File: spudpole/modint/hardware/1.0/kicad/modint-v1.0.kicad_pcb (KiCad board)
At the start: 2 copper layers, 87.6 x 120.7 mm, 35 parts, among them J1 SENSOR, J2 DK ST, J3 NMEA, J4 UP DN, K1 SANYOU-SRD, K2 SANYOU-SRD, Q1 2N2219, Q2 2N2219, SW1 INSTANCE, U1 4N25, U2 4N25, U3 Teensy_3.2, U4 TEN20-2421WIN, U5 MCP2551-I-P

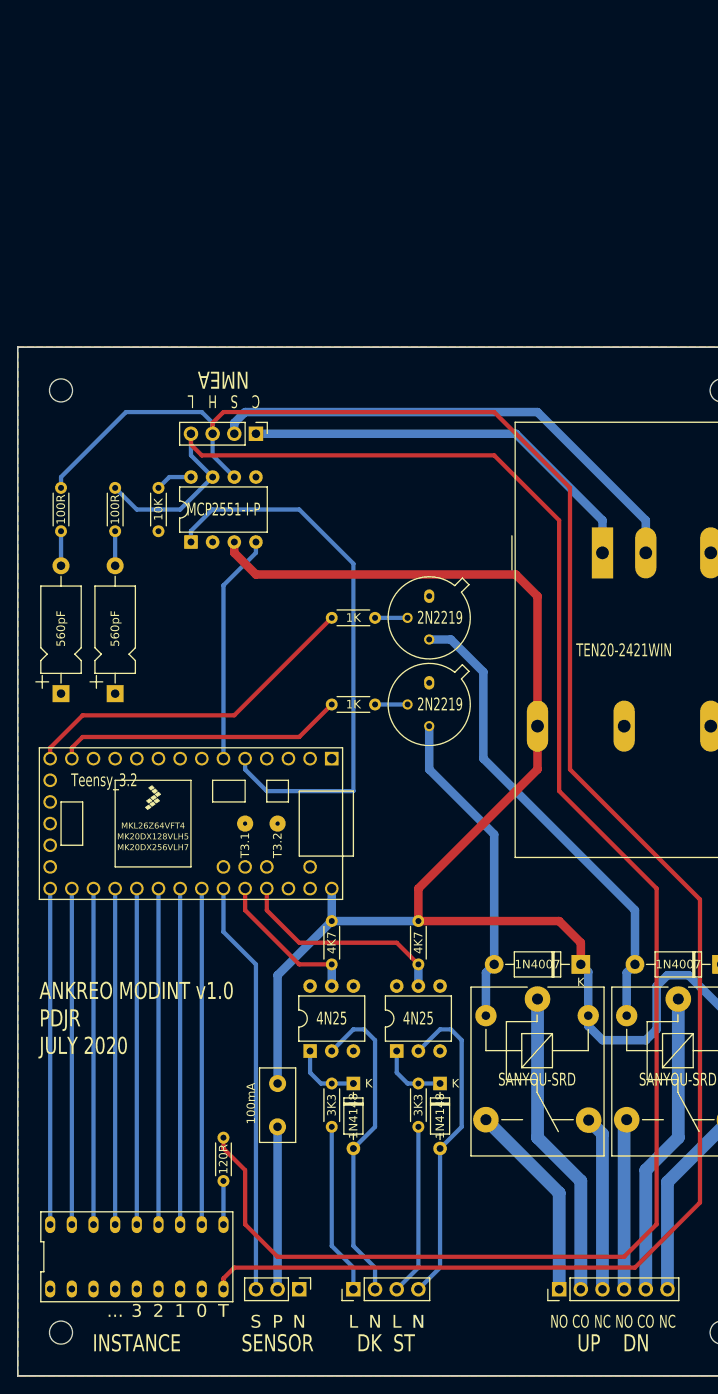
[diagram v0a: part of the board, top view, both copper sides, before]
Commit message: Added relay state LEDs to schematic
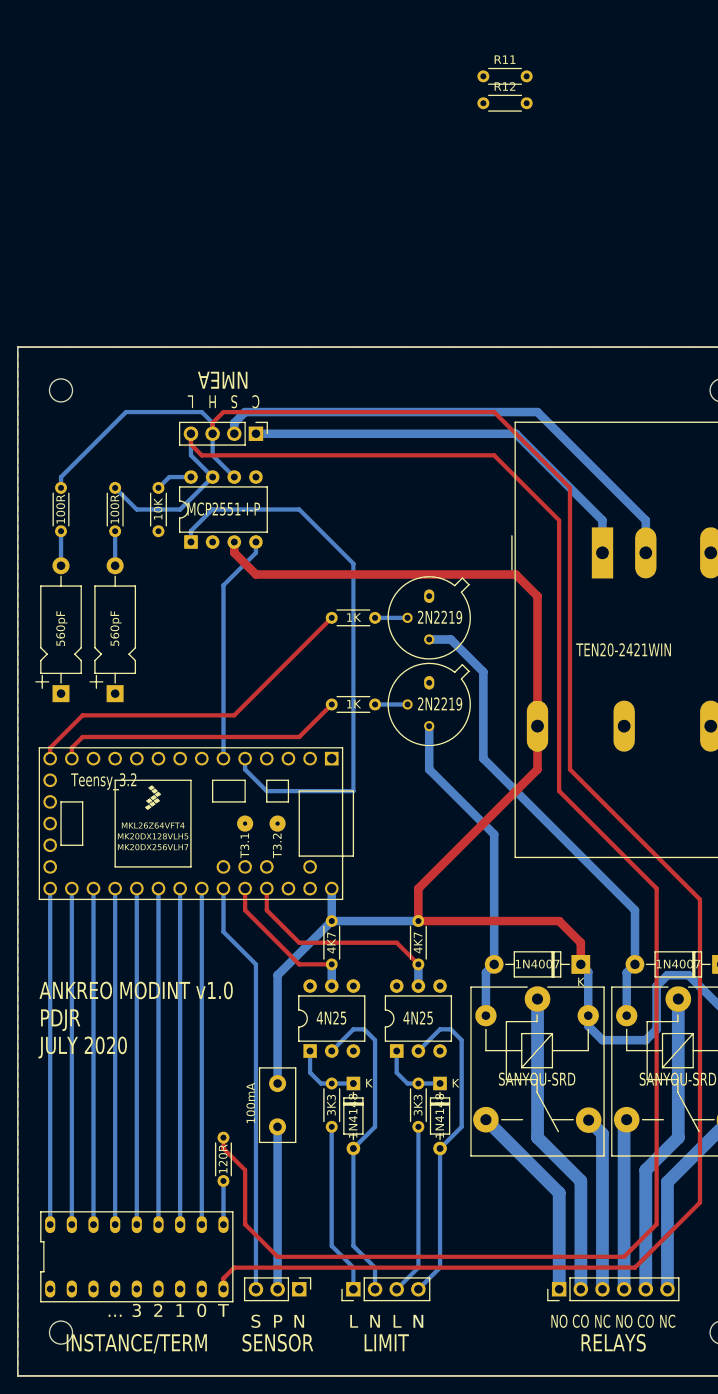
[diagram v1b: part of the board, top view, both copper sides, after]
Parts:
- added R11: 1K, Resistor_THT:R_Axial_DIN0204_L3.6mm_D1.6mm_P5.08mm_Horizontal, F.Cu at (101.6, 14.0)
- added R12: 1K, Resistor_THT:R_Axial_DIN0204_L3.6mm_D1.6mm_P5.08mm_Horizontal, F.Cu at (101.6, 17.1)
- J2: value DK ST -> LIMIT
- J4: value UP DN -> RELAYS
- SW1: value INSTANCE -> INSTANCE/TERM
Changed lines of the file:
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@@
     (tracks 172)
     (zones 0)
-    (modules 35)
+    (modules 37)
     (nets 43)
   )
@@
   )
   (setup
-    (last_trace_width 1)
+    (last_trace_width 0.25)
     (user_trace_width 0.5)
     (user_trace_width 1)
@@
     (add_net "Net-(D3-Pad2)")
     (add_net "Net-(D4-Pad2)")
+    (add_net "Net-(D5-Pad2)")
+    (add_net "Net-(D6-Pad2)")
     (add_net "Net-(F1-Pad2)")
     (add_net "Net-(J1-Pad3)")
@@
     (add_net "Net-(SW1-Pad17)")
     (add_net "Net-(SW1-Pad18)")
+    (add_net "Net-(U1-Pad3)")
+    (add_net "Net-(U1-Pad6)")
+    (add_net "Net-(U2-Pad3)")
+    (add_net "Net-(U2-Pad6)")
+    (add_net "Net-(U3-Pad10)")
+    (add_net "Net-(U3-Pad11)")
+    (add_net "Net-(U3-Pad12)")
+    (add_net "Net-(U3-Pad2)")
+    (add_net "Net-(U3-Pad26)")
+    (add_net "Net-(U3-Pad27)")
+    (add_net "Net-(U3-Pad29)")
+    (add_net "Net-(U3-Pad3)")
+    (add_net "Net-(U3-Pad30)")
+    (add_net "Net-(U3-Pad31)")
+    (add_net "Net-(U3-Pad32)")
+    (add_net "Net-(U3-Pad33)")
+    (add_net "Net-(U3-Pad4)")
     (add_net "Net-(U3-Pad5)")
     (add_net "Net-(U3-Pad6)")
+    (add_net "Net-(U3-Pad7)")
+    (add_net "Net-(U3-Pad8)")
+    (add_net "Net-(U3-Pad9)")
+    (add_net "Net-(U4-Pad4)")
+    (add_net "Net-(U4-Pad6)")
+    (add_net "Net-(U5-Pad5)")
+  )
+  (module Resistor_THT:R_Axial_DIN0204_L3.6mm_D1.6mm_P5.08mm_Horizontal (layer F.Cu)
+    (at 101.6 17.12)
+    (descr "Resistor, Axial_DIN0204 series, Axial, Horizontal, pin pitch=5.08mm, 0.167W, length*diameter=3.6*1.6mm^2, http://cdn-reichelt.de/documents/datenblatt/B400/1_4W%23YAG.pdf")
+    (tags "Resistor Axial_DIN0204 series Axial Horizontal pin pitch 5.08mm 0.167W length 3.6mm diameter 1.6mm")
+    (fp_text reference R12 (at 2.54 -1.92) (layer F.SilkS)
+      (effects (font (size 1 1) (thickness 0.15)))
+    )
+    (fp_text value 1K (at 2.54 1.92) (layer F.Fab)
+      (effects (font (size 1 1) (thickness 0.15)))
+    )
+    (fp_text user %R (at 2.54 0) (layer F.Fab)
+      (effects (font (size 0.72 0.72) (thickness 0.108)))
+    )
+    (fp_line (start 6.03 -1.05) (end -0.95 -1.05) (layer F.CrtYd) (width 0.05))
+    (fp_line (start 6.03 1.05) (end 6.03 -1.05) (layer F.CrtYd) (width 0.05))
+    (fp_line (start -0.95 1.05) (end 6.03 1.05) (layer F.CrtYd) (width 0.05))
+    (fp_line (start -0.95 -1.05) (end -0.95 1.05) (layer F.CrtYd) (width 0.05))
+    (fp_line (start 0.62 0.92) (end 4.46 0.92) (layer F.SilkS) (width 0.12))
+    (fp_line (start 0.62 -0.92) (end 4.46 -0.92) (layer F.SilkS) (width 0.12))
+    (fp_line (start 5.08 0) (end 4.34 0) (layer F.Fab) (width 0.1))
+    (fp_line (start 0 0) (end 0.74 0) (layer F.Fab) (width 0.1))
+    (fp_line (start 4.34 -0.8) (end 0.74 -0.8) (layer F.Fab) (width 0.1))
+    (fp_line (start 4.34 0.8) (end 4.34 -0.8) (layer F.Fab) (width 0.1))
+    (fp_line (start 0.74 0.8) (end 4.34 0.8) (layer F.Fab) (width 0.1))
+    (fp_line (start 0.74 -0.8) (end 0.74 0.8) (layer F.Fab) (width 0.1))
+    (pad 2 thru_hole oval (at 5.08 0) (size 1.4 1.4) (drill 0.7) (layers *.Cu *.Mask)
+      (net 4 "Net-(D3-Pad1)"))
+    (pad 1 thru_hole circle (at 0 0) (size 1.4 1.4) (drill 0.7) (layers *.Cu *.Mask))
+    (model ${KISYS3DMOD}/Resistor_THT.3dshapes/R_Axial_DIN0204_L3.6mm_D1.6mm_P5.08mm_Horizontal.wrl
+      (at (xyz 0 0 0))
+      (scale (xyz 1 1 1))
+      (rotate (xyz 0 0 0))
+    )
+  )
+  (module Resistor_THT:R_Axial_DIN0204_L3.6mm_D1.6mm_P5.08mm_Horizontal (layer F.Cu)
+    (at 101.6 13.97)
+    (descr "Resistor, Axial_DIN0204 series, Axial, Horizontal, pin pitch=5.08mm, 0.167W, length*diameter=3.6*1.6mm^2, http://cdn-reichelt.de/documents/datenblatt/B400/1_4W%23YAG.pdf")
+    (tags "Resistor Axial_DIN0204 series Axial Horizontal pin pitch 5.08mm 0.167W length 3.6mm diameter 1.6mm")
+    (fp_text reference R11 (at 2.54 -1.92) (layer F.SilkS)
+      (effects (font (size 1 1) (thickness 0.15)))
+    )
+    (fp_text value 1K (at 2.54 1.92) (layer F.Fab)
+      (effects (font (size 1 1) (thickness 0.15)))
+    )
+    (fp_text user %R (at 2.54 0) (layer F.Fab)
+      (effects (font (size 0.72 0.72) (thickness 0.108)))
+    )
+    (fp_line (start 6.03 -1.05) (end -0.95 -1.05) (layer F.CrtYd) (width 0.05))
+    (fp_line (start 6.03 1.05) (end 6.03 -1.05) (layer F.CrtYd) (width 0.05))
+    (fp_line (start -0.95 1.05) (end 6.03 1.05) (layer F.CrtYd) (width 0.05))
+    (fp_line (start -0.95 -1.05) (end -0.95 1.05) (layer F.CrtYd) (width 0.05))
+    (fp_line (start 0.62 0.92) (end 4.46 0.92) (layer F.SilkS) (width 0.12))
+    (fp_line (start 0.62 -0.92) (end 4.46 -0.92) (layer F.SilkS) (width 0.12))
+    (fp_line (start 5.08 0) (end 4.34 0) (layer F.Fab) (width 0.1))
+    (fp_line (start 0 0) (end 0.74 0) (layer F.Fab) (width 0.1))
+    (fp_line (start 4.34 -0.8) (end 0.74 -0.8) (layer F.Fab) (width 0.1))
+    (fp_line (start 4.34 0.8) (end 4.34 -0.8) (layer F.Fab) (width 0.1))
+    (fp_line (start 0.74 0.8) (end 4.34 0.8) (layer F.Fab) (width 0.1))
+    (fp_line (start 0.74 -0.8) (end 0.74 0.8) (layer F.Fab) (width 0.1))
+    (pad 2 thru_hole oval (at 5.08 0) (size 1.4 1.4) (drill 0.7) (layers *.Cu *.Mask)
+      (net 4 "Net-(D3-Pad1)"))
+    (pad 1 thru_hole circle (at 0 0) (size 1.4 1.4) (drill 0.7) (layers *.Cu *.Mask))
+    (model ${KISYS3DMOD}/Resistor_THT.3dshapes/R_Axial_DIN0204_L3.6mm_D1.6mm_P5.08mm_Horizontal.wrl
+      (at (xyz 0 0 0))
+      (scale (xyz 1 1 1))
+      (rotate (xyz 0 0 0))
+    )
   )
   (module PDJR:DIP-18_297_ELL (layer F.Cu)
@@
       (effects (font (size 1 1) (thickness 0.15)))
     )
-    (fp_text value INSTANCE (at 0 10.16) (layer F.SilkS)
+    (fp_text value INSTANCE/TERM (at 0 10.16) (layer F.SilkS)
       (effects (font (size 2 1.5) (thickness 0.2)))
     )
@@
       (effects (font (size 2 1.5) (thickness 0.15)))
     )
-    (fp_text value "DK  ST" (at -6.35 3.81 180) (layer F.SilkS)
+    (fp_text value LIMIT (at -6.35 3.81 180) (layer F.SilkS)
       (effects (font (size 2 1.5) (thickness 0.2)))
     )
@@
       (effects (font (size 1 1) (thickness 0.15)))
     )
-    (fp_text value "UP    DN" (at -6.35 6.35 180) (layer F.SilkS)
+    (fp_text value RELAYS (at -6.35 6.35 180) (layer F.SilkS)
       (effects (font (size 2 1.5) (thickness 0.2)))
     )
@@
   (segment (start 76.2 111.76) (end 80.01 115.57) (width 0.5) (layer F.Cu) (net 9))
   (segment (start 93.98 118.11) (end 93.98 120.65) (width 1) (layer B.Cu) (net 9) (status 30))
-  (segment (start 50.8 148.59) (end 50.8 109.22) (width 0.5) (layer B.Cu) (net 42) (status 30))
-  (segment (start 53.34 148.59) (end 53.34 109.22) (width 0.5) (layer B.Cu) (net 41) (status 30))
   (segment (start 55.88 109.22) (end 55.88 148.59) (width 0.5) (layer B.Cu) (net 10) (status 30))
   (segment (start 58.42 148.59) (end 58.42 109.22) (width 0.5) (layer B.Cu) (net 11) (status 30))
@@
   (segment (start 67.31 58.42) (end 69.85 60.96) (width 0.5) (layer B.Cu) (net 29) (status 20))
   (segment (start 67.31 55.88) (end 67.31 58.42) (width 0.5) (layer B.Cu) (net 29) (status 10))
+  (segment (start 67.31 57.15) (end 67.31 55.88) (width 0.5) (layer F.Cu) (net 29))
+  (segment (start 68.58 58.42) (end 67.31 57.15) (width 0.5) (layer F.Cu) (net 29))
+  (segment (start 73.66 148.59) (end 77.47 152.4) (width 0.5) (layer F.Cu) (net 29))
+  (segment (start 73.66 142.24) (end 73.66 148.59) (width 0.5) (layer F.Cu) (net 29))
+  (segment (start 71.12 139.7) (end 73.66 142.24) (width 0.5) (layer F.Cu) (net 29))
+  (segment (start 71.12 138.43) (end 71.12 139.7) (width 0.5) (layer F.Cu) (net 29))
+  (segment (start 118.11 152.4) (end 121.92 148.59) (width 0.5) (layer F.Cu) (net 29))
+  (segment (start 77.47 152.4) (end 118.11 152.4) (width 0.5) (layer F.Cu) (net 29))
+  (segment (start 121.92 148.59) (end 121.92 109.22) (width 0.5) (layer F.Cu) (net 29))
+  (segment (start 121.92 109.22) (end 110.49 97.79) (width 0.5) (layer F.Cu) (net 29))
+  (segment (start 110.49 97.79) (end 110.49 66.04) (width 0.5) (layer F.Cu) (net 29))
+  (segment (start 110.49 66.04) (end 102.87 58.42) (width 0.5) (layer F.Cu) (net 29))
+  (segment (start 102.87 58.42) (end 68.58 58.42) (width 0.5) (layer F.Cu) (net 29))
   (segment (start 72.39 55.88) (end 72.39 54.61) (width 1) (layer B.Cu) (net 30) (status 10))
   (segment (start 72.39 54.61) (end 73.66 53.34) (width 1) (layer B.Cu) (net 30))
@@
   (segment (start 74.93 69.85) (end 74.93 68.58) (width 0.5) (layer B.Cu) (net 39) (status 20))
   (segment (start 71.12 73.66) (end 74.93 69.85) (width 0.5) (layer B.Cu) (net 39))
-  (segment (start 67.31 57.15) (end 67.31 55.88) (width 0.5) (layer F.Cu) (net 29))
-  (segment (start 68.58 58.42) (end 67.31 57.15) (width 0.5) (layer F.Cu) (net 29))
-  (segment (start 73.66 148.59) (end 77.47 152.4) (width 0.5) (layer F.Cu) (net 29))
-  (segment (start 73.66 142.24) (end 73.66 148.59) (width 0.5) (layer F.Cu) (net 29))
-  (segment (start 71.12 139.7) (end 73.66 142.24) (width 0.5) (layer F.Cu) (net 29))
-  (segment (start 71.12 138.43) (end 71.12 139.7) (width 0.5) (layer F.Cu) (net 29))
-  (segment (start 118.11 152.4) (end 121.92 148.59) (width 0.5) (layer F.Cu) (net 29))
-  (segment (start 77.47 152.4) (end 118.11 152.4) (width 0.5) (layer F.Cu) (net 29))
-  (segment (start 121.92 148.59) (end 121.92 109.22) (width 0.5) (layer F.Cu) (net 29))
-  (segment (start 121.92 109.22) (end 110.49 97.79) (width 0.5) (layer F.Cu) (net 29))
-  (segment (start 110.49 97.79) (end 110.49 66.04) (width 0.5) (layer F.Cu) (net 29))
-  (segment (start 110.49 66.04) (end 102.87 58.42) (width 0.5) (layer F.Cu) (net 29))
-  (segment (start 102.87 58.42) (end 68.58 58.42) (width 0.5) (layer F.Cu) (net 29))
   (segment (start 71.12 148.625) (end 71.12 143.51) (width 0.5) (layer B.Cu) (net 40))
+  (segment (start 53.34 148.59) (end 53.34 109.22) (width 0.5) (layer B.Cu) (net 41) (status 30))
+  (segment (start 50.8 148.59) (end 50.8 109.22) (width 0.5) (layer B.Cu) (net 42) (status 30))
   (zone (net 16) (net_name GND) (layer F.Cu) (hatch edge 0.508)
     (connect_pads (clearance 0.508))

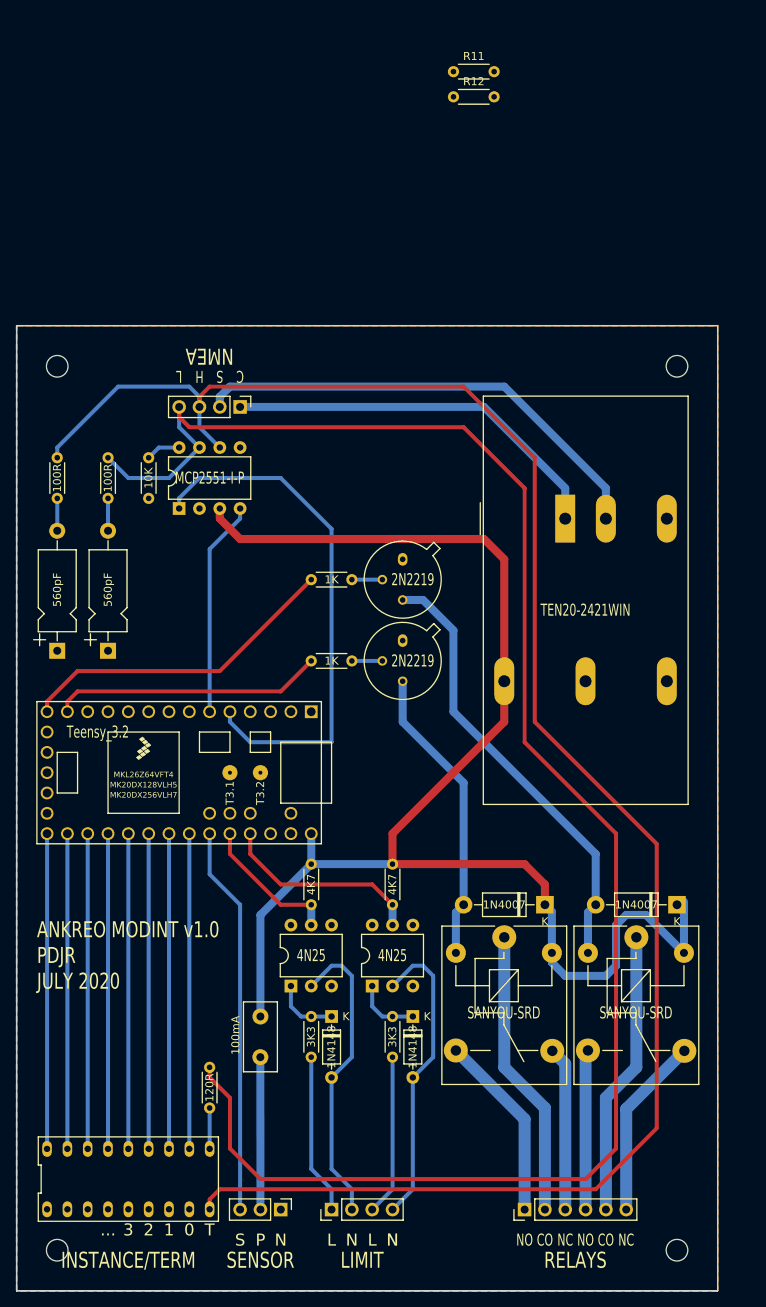
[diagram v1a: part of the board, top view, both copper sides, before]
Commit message: Revised PCB layout
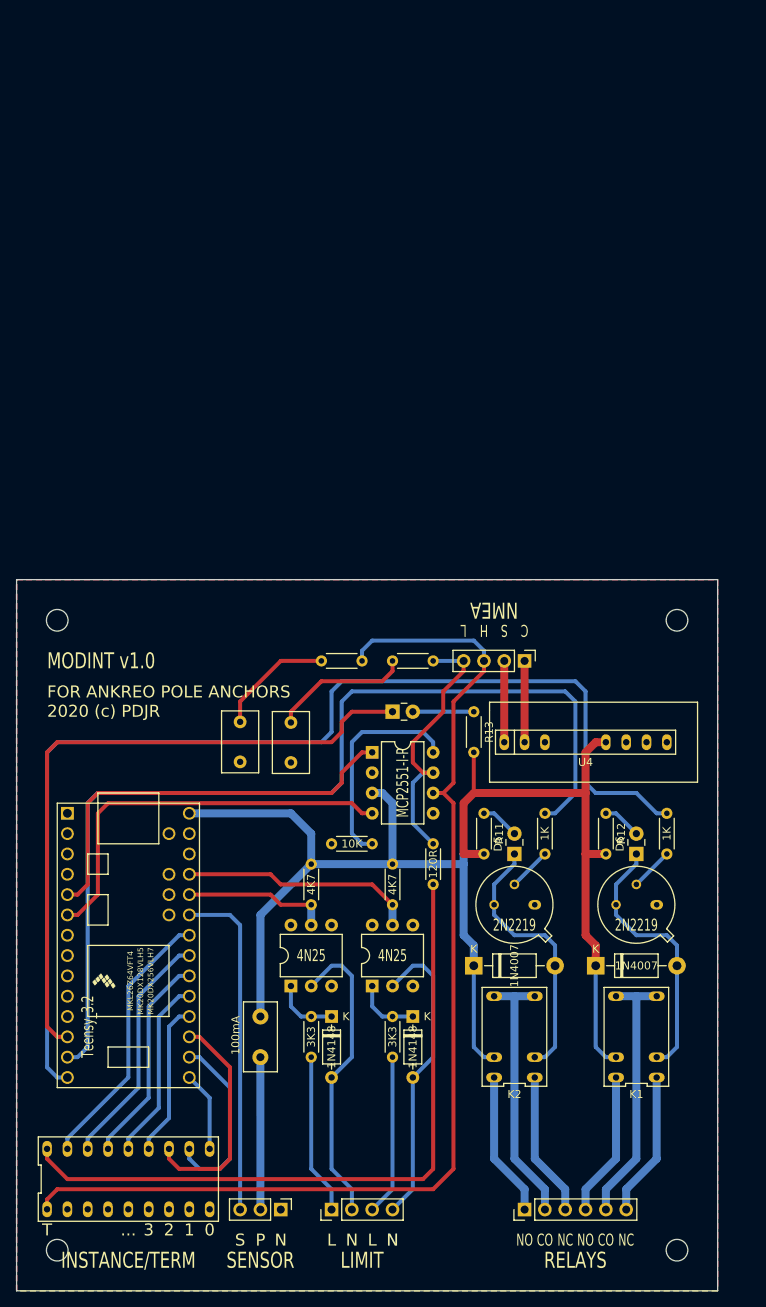
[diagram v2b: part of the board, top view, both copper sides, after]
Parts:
- added D5: LED, LED_THT:LED_Rectangular_W3.0mm_H2.0mm, F.Cu at (109.2, 111.8)
- added D6: LED, LED_THT:LED_Rectangular_W3.0mm_H2.0mm, F.Cu at (124.5, 111.8)
- added D7: LED, LED_THT:LED_Rectangular_W3.0mm_H2.0mm, F.Cu at (94.0, 94.0)
- added R13: 1K, Resistor_THT:R_Axial_DIN0204_L3.6mm_D1.6mm_P5.08mm_Horizontal, F.Cu at (104.1, 94.0)
- C1, C2: footprint Capacitor_THT:CP_Axial_L10.0mm_D4.5mm_P15.00mm_Horizontal -> Capacitor_THT:C_Disc_D7.5mm_W4.4mm_P5.00mm
- K1, K2: value SANYOU-SRD -> SANYOU_SRD_Form_C; footprint Relay_THT:Relay_SPDT_SANYOU_SRD_Series_Form_C -> PDJR:RS_RELAY_476-757
- U4: value TEN20-2421WIN -> TEC2-2411WI; footprint Converter_DCDC:Converter_DCDC_TRACO_TEN20-xxxx_THT -> PDJR:TMR_2-2411WI
- moved R11 92.8 mm to (105.4, 106.7), turned to 270 degrees
- moved R12 91.6 mm to (120.7, 106.7), turned to 270 degrees
- moved Q1 53.6 mm to (127.0, 118.1), turned to 180 degrees
- moved R5 52.2 mm to (128.3, 111.8), turned to 90 degrees
- moved R7 48.9 mm to (86.4, 110.5), turned to 0 degrees
- moved J3 47.7 mm to (110.5, 87.6)
- moved R8 45.8 mm to (90.2, 87.6), turned to 180 degrees
- moved R9 41.0 mm to (94.0, 87.6), turned to 0 degrees
- moved R10 39.5 mm to (99.1, 110.5)
- moved U5 38.9 mm to (91.4, 99.1), turned to 0 degrees
- moved Q2 36.9 mm to (111.8, 118.1), turned to 180 degrees
- moved R6 34.1 mm to (113.0, 111.8), turned to 90 degrees
- moved REF** 31.8 mm to (129.5, 82.5)
- moved REF** 31.8 mm to (52.1, 82.5)
- moved U4 28.1 mm to (118.1, 97.8)
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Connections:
- K1 pad 1: Net-(J4-Pad5) -> Net-(J4-Pad6)
- K1 pad 5: Net-(D3-Pad1) -> Net-(J4-Pad5)
- K2 pad 1: Net-(J4-Pad2) -> Net-(J4-Pad3)
- K2 pad 5: Net-(D3-Pad1) -> Net-(J4-Pad2)
- R11 pad 1: (no net) -> Net-(D5-Pad2)
- R12 pad 1: (no net) -> Net-(D6-Pad2)
- SW1 pad 1: GND -> Net-(J3-Pad3)
- SW1 pad 10: Net-(R10-Pad2) -> Net-(SW1-Pad10)
- SW1 pad 18: Net-(SW1-Pad18) -> Net-(R10-Pad2)
- SW1 pad 9: Net-(J3-Pad3) -> GND
- U3 pad 12: (no net) -> Net-(D7-Pad1)
- U3 pad 15: Net-(SW1-Pad18) -> Net-(SW1-Pad10)
- U3 pad 16: Net-(SW1-Pad17) -> Net-(SW1-Pad11)
- U3 pad 17: Net-(SW1-Pad16) -> Net-(SW1-Pad12)
- U3 pad 18: Net-(SW1-Pad15) -> Net-(SW1-Pad13)
- U3 pad 20: Net-(SW1-Pad13) -> Net-(SW1-Pad15)
- U3 pad 21: Net-(SW1-Pad12) -> Net-(SW1-Pad16)
- U3 pad 22: Net-(SW1-Pad11) -> Net-(SW1-Pad17)
- U4 pad 1: Net-(J3-Pad1) -> Net-(J3-Pad2)
- U4 pad 2: Net-(J3-Pad2) -> Net-(J3-Pad1)
- U4 pad 3: Net-(D3-Pad1) -> (no net)
- U4 pad 6: (no net) -> Net-(D3-Pad1)
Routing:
- net Net-(J3-Pad4): track 218.2 -> 33.9 mm
- net Net-(R5-Pad2): track 40.6 -> 140.1 mm
- net Net-(R6-Pad2): track 33.9 -> 123.1 mm
- net Net-(J3-Pad3): track 228.5 -> 139.8 mm
- net Net-(D7-Pad1): track 0.00 -> 83.4 mm
- net Net-(R10-Pad2): track 5.12 -> 86.6 mm
- net Net-(J3-Pad2): track 59.1 -> 10.2 mm
- net Net-(SW1-Pad18): track 39.4 -> 0.00 mm
- net Net-(J3-Pad1): track 48.7 -> 10.2 mm
- net Net-(U3-Pad6): track 27.0 -> 50.4 mm
- net Net-(R7-Pad2): track 4.34 -> 27.0 mm
- net Net-(D3-Pad2): track 56.0 -> 33.6 mm
- net Net-(SW1-Pad13): track 39.4 -> 19.4 mm
- net Net-(SW1-Pad11): track 39.4 -> 22.9 mm
- net Net-(SW1-Pad14): track 39.4 -> 23.0 mm
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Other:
- board size 87.6 x 120.7 mm -> 87.6 x 88.9 mm
- board text added: "FOR ANKREO POLE ANCHORS 2020 (c) PDJR"
- board text added: "MODINT v1.0"
- board text removed: "ANKREO MODINT v1.0 PDJR JULY 2020"
